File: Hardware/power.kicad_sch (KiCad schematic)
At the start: 0 parts

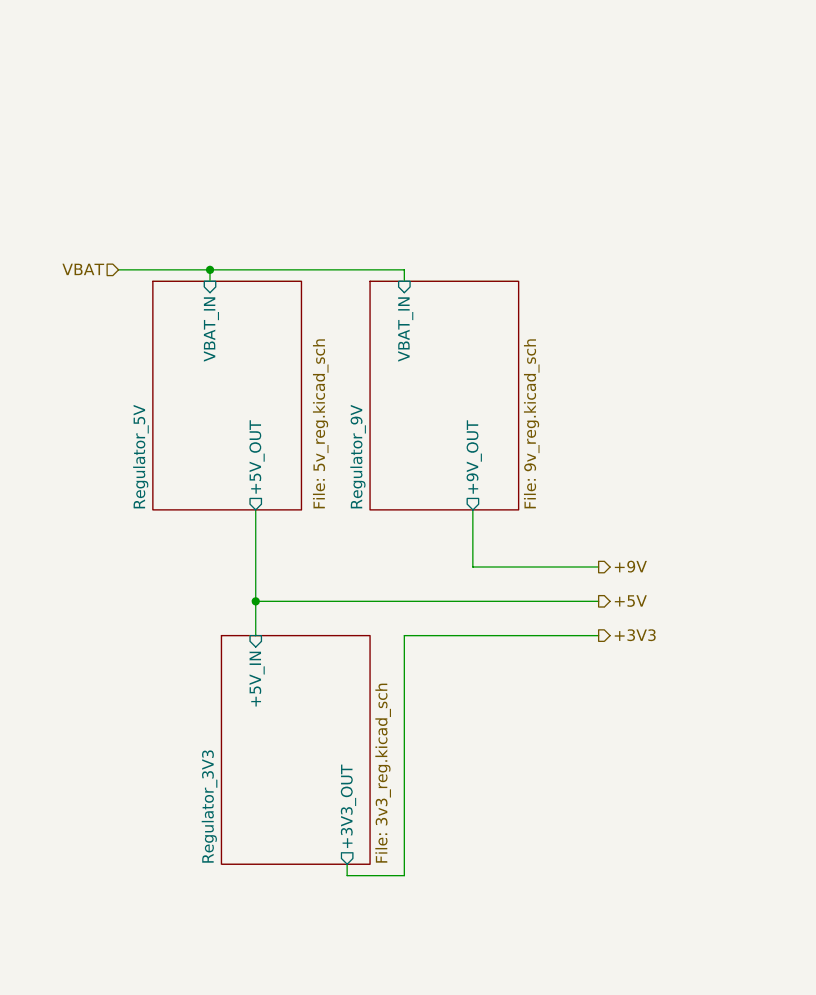
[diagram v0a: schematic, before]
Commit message: Finalize schematic: Add connectors, LEDs, Buzzer and fix all ERC errors
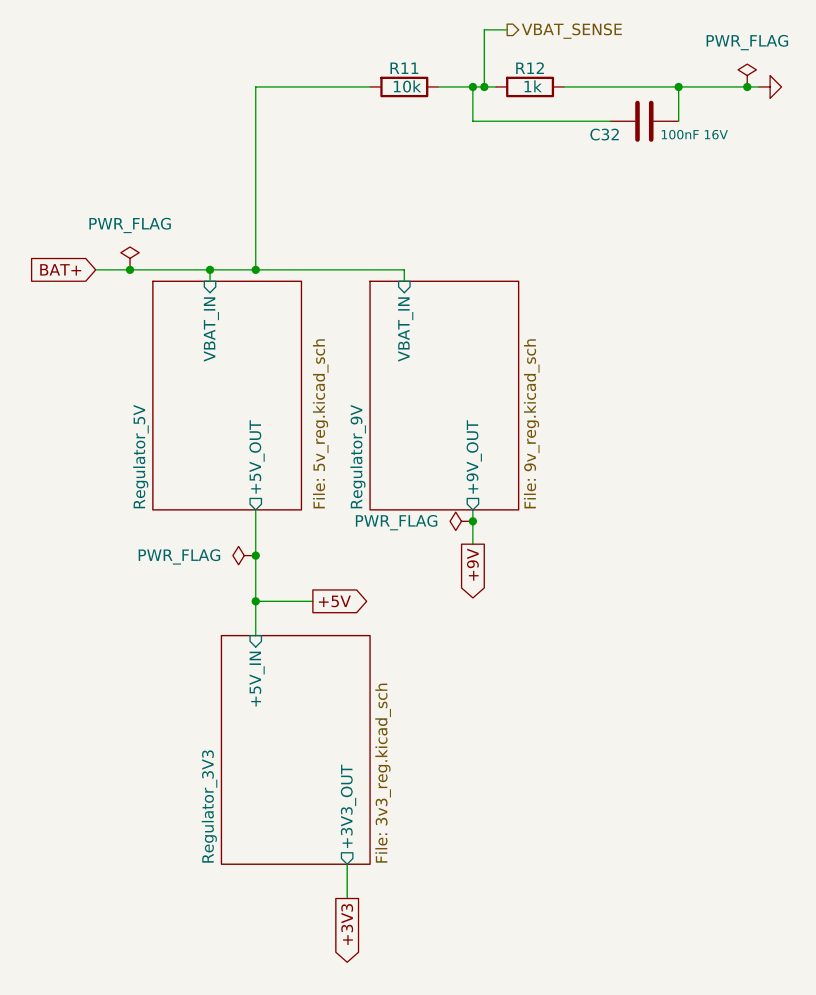
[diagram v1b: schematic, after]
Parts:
- added C32: 100nF 16V, symbol Device:C
- added R11: 10k, symbol Device:R
- added R12: 1k, symbol Device:R
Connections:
- new net BAT+: R11.2
- new net GND: C32.1, R12.1
- new net VBAT_SENSE: C32.2, R11.1, R12.2

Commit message: Finalize component placement and silkscreen
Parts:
- C32: footprint (none) -> Capacitor_SMD:C_0402_1005Metric
- R11, R12: footprint (none) -> Resistor_SMD:R_0402_1005Metric
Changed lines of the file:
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@@
 			)
 		)
-		(property "Footprint" ""
+		(property "Footprint" "Resistor_SMD:R_0402_1005Metric"
 			(at 80.01 26.162 90)
 			(effects
@@
 			)
 		)
-		(property "Footprint" ""
+		(property "Footprint" "Resistor_SMD:R_0402_1005Metric"
 			(at 66.04 26.162 90)
 			(effects
@@
 			)
 		)
-		(property "Footprint" ""
+		(property "Footprint" "Capacitor_SMD:C_0402_1005Metric"
 			(at 88.9 32.7152 0)
 			(effects
